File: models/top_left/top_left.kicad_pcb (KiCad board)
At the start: 2 copper layers, 145.3 x 102.4 mm, 35 parts, among them SW0_1 SW_Push, SW0_2 SW_Push, SW0_3 SW_Push, SW0_4 SW_Push, SW1_0 SW_Push, SW1_2 SW_Push, SW1_3 SW_Push, SW1_4 SW_Push, SW1_5 SW_Push, SW2_0 SW_Push, SW2_1 SW_Push, SW2_3 SW_Push, SW2_4 SW_Push, SW2_5 SW_Push, SW3_0 SW_Push, SW3_1 SW_Push, SW3_2 SW_Push, SW3_4 SW_Push, SW4_0 SW_Push, SW4_1 SW_Push, SW4_2 SW_Push, SW4_3 SW_Push, SW5_0 SW_Push, SW5_1 SW_Push, SW5_2 SW_Push, SW5_3 SW_Push, SW5_4 SW_Push, SW6_0 SW_Push, SW6_1 SW_Push, SW6_2 SW_Push, SW6_3 SW_Push, SW6_4 SW_Push

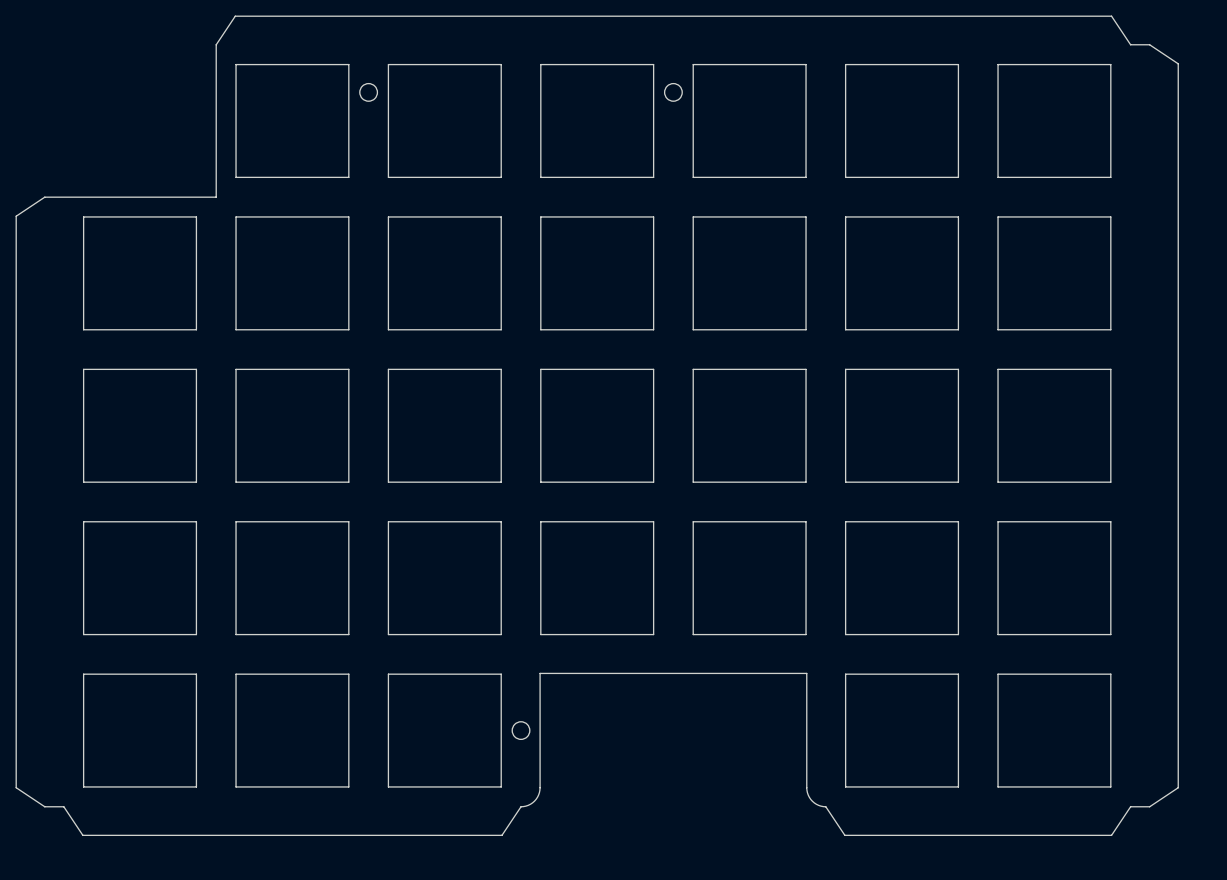
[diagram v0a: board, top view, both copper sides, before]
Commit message: feat: added several 3D models
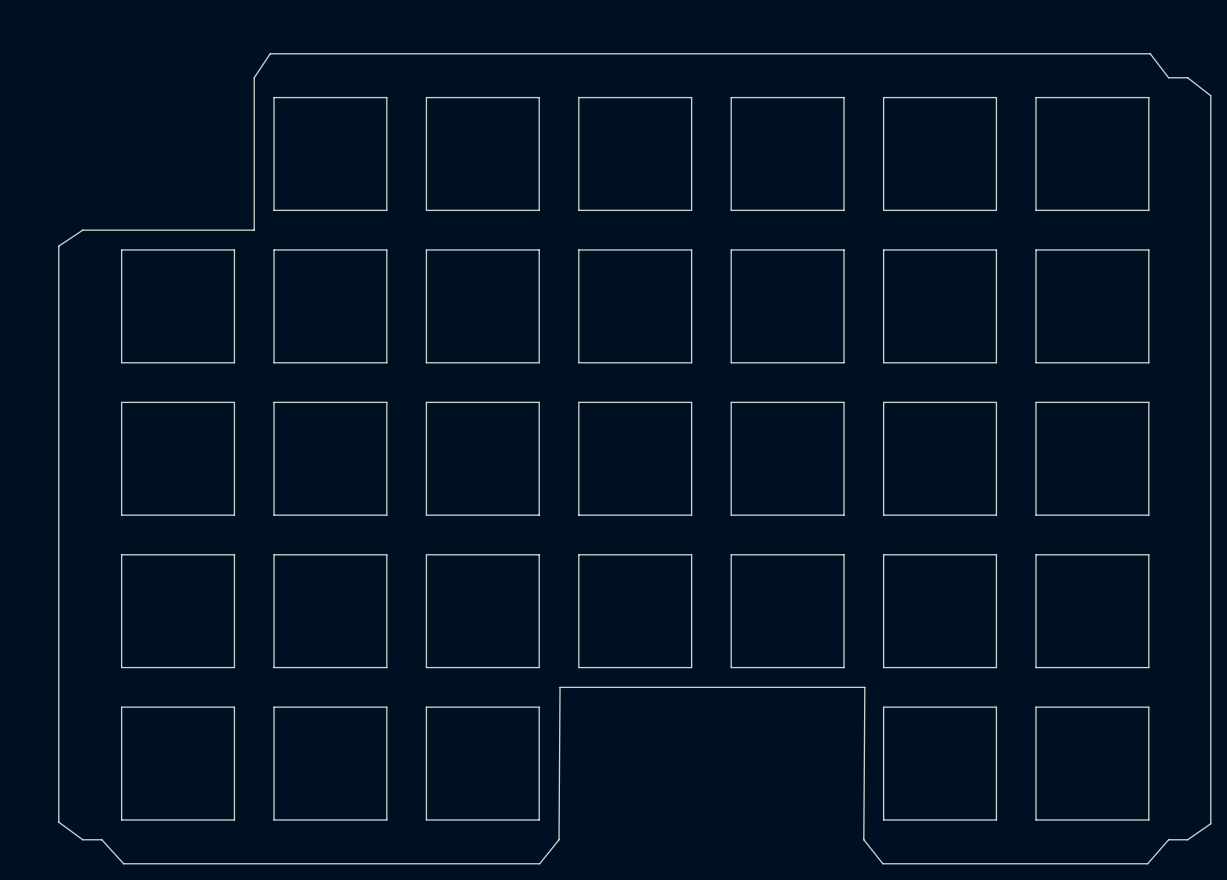
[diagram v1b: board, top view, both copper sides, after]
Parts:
- removed Ref** (x3): Val**, sym6_salicyl:m2_Screw_Hole
- moved SW0_1 6.29 mm to (111.9, 80.3)
- moved SW0_2 6.29 mm to (226.2, 80.3)
- moved SW0_3 6.29 mm to (207.2, 99.4)
- moved SW0_4 6.29 mm to (188.1, 118.4)
- moved SW1_0 6.29 mm to (131.0, 61.3)
- moved SW1_2 6.29 mm to (111.9, 99.4)
- moved SW1_3 6.29 mm to (226.2, 99.4)
- moved SW1_4 6.29 mm to (207.2, 118.4)
- moved SW1_5 6.29 mm to (207.2, 137.5)
- moved SW2_0 6.29 mm to (150.0, 61.3)
- moved SW2_1 6.29 mm to (131.0, 80.3)
- moved SW2_3 6.29 mm to (111.9, 118.4)
- moved SW2_4 6.29 mm to (226.2, 118.4)
- moved SW2_5 6.29 mm to (226.2, 137.5)
- moved SW3_0 6.29 mm to (169.1, 61.3)
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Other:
- board size 145.3 x 102.4 mm -> 144 x 101.2 mm
